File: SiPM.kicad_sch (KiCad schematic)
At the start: 10 parts, among them U27 LTC2487

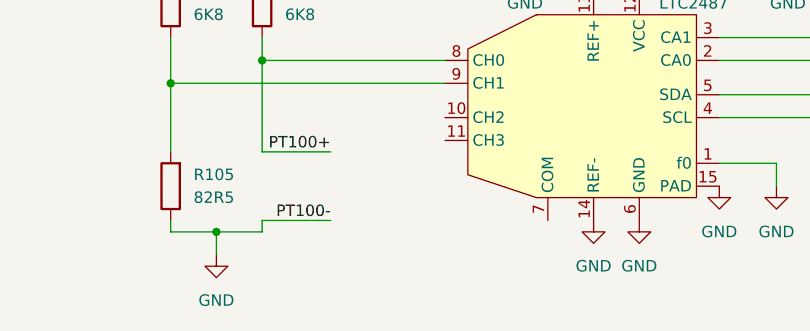
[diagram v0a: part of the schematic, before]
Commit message: gnd and gnda
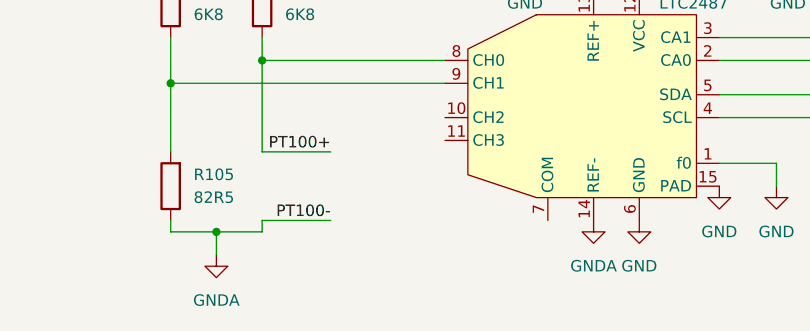
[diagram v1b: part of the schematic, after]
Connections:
- net GND: no longer R105.1, SiPM4.24 (NTC2), U27.14 (REF-)
- net GNDA: now also R105.1, SiPM4.24 (NTC2), U27.14 (REF-)
